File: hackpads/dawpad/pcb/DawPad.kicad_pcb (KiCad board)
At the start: 2 copper layers, 98.5 x 81.5 mm, 32 parts, among them SW1 SW_Push, SW10 SW_Push, SW11 SW_Push, SW12 SW_Push, SW13 RotaryEncoder_Switch_MP, SW14 RotaryEncoder_Switch_MP, SW15 RotaryEncoder_Switch_MP, SW16 RotaryEncoder_Switch_MP, SW2 SW_Push, SW3 SW_Push, SW4 SW_Push, SW5 SW_Push, SW6 SW_Push, SW7 SW_Push, SW8 SW_Push, SW9 SW_Push, U1 XIAO-RP2040-DIP, U2 MCP23017_SO

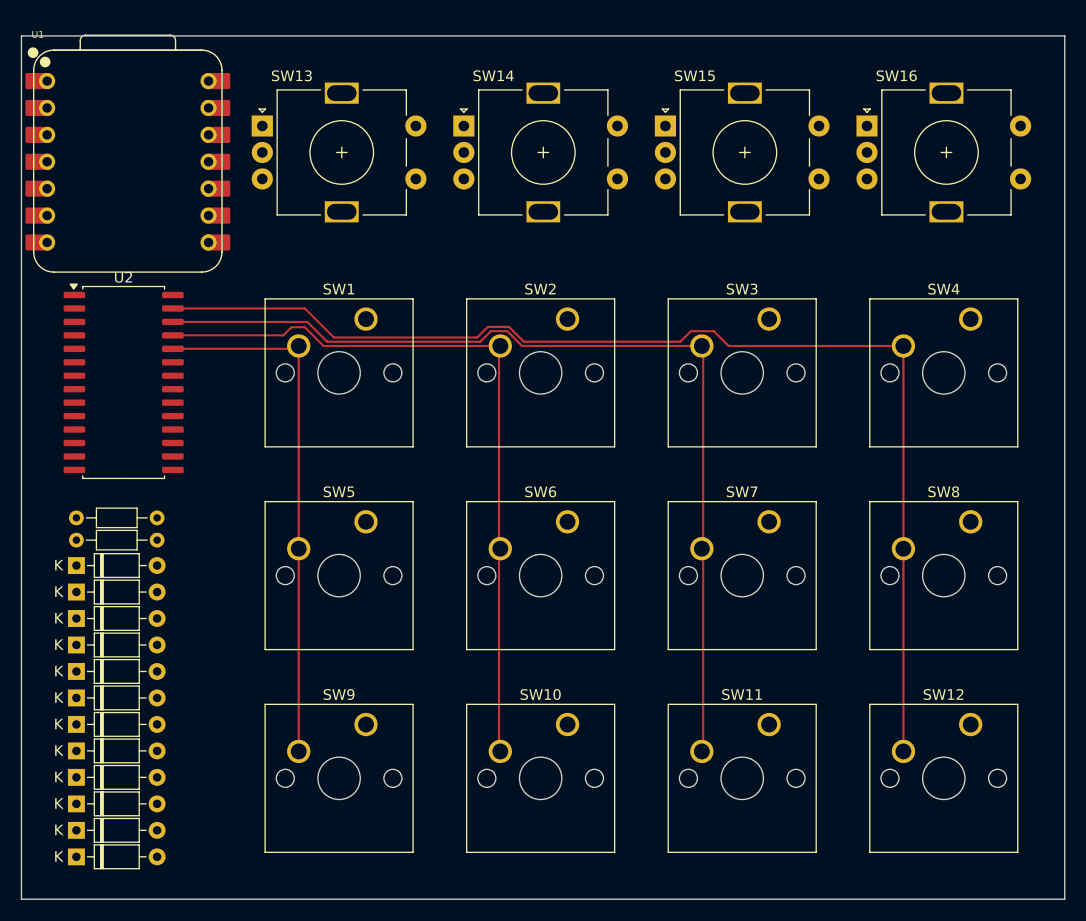
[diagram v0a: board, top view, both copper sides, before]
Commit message: Add LEDs to and finish PCB for DawPad
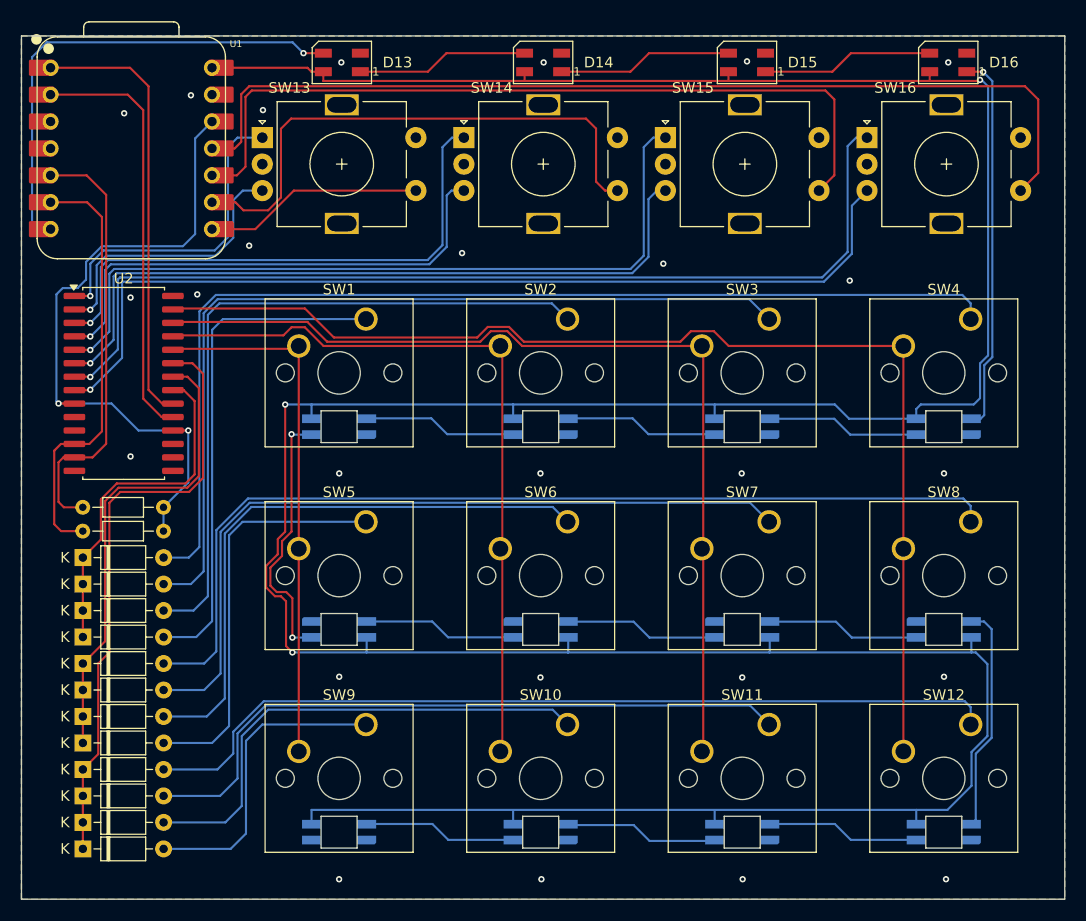
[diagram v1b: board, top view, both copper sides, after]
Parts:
- added D13: SK6812MINI, LED_SMD:LED_SK6812MINI_PLCC4_3.5x3.5mm_P1.75mm, F.Cu at (45.2, 17.5)
- added D14: SK6812MINI, LED_SMD:LED_SK6812MINI_PLCC4_3.5x3.5mm_P1.75mm, F.Cu at (64.2, 17.5)
- added D15: SK6812MINI, LED_SMD:LED_SK6812MINI_PLCC4_3.5x3.5mm_P1.75mm, F.Cu at (83.5, 17.5)
- added D16: SK6812MINI, LED_SMD:LED_SK6812MINI_PLCC4_3.5x3.5mm_P1.75mm, F.Cu at (102.5, 17.5)
- added D17: SK6812MINI, SK6812MINI-E:SK6812MINI-E, B.Cu at (102.1, 51.9)
- added D18: SK6812MINI, SK6812MINI-E:SK6812MINI-E, B.Cu at (83.0, 51.9)
- added D19: SK6812MINI, SK6812MINI-E:SK6812MINI-E, B.Cu at (64.0, 51.9)
- added D20: SK6812MINI, SK6812MINI-E:SK6812MINI-E, B.Cu at (45.0, 51.9)
- added D21: SK6812MINI, SK6812MINI-E:SK6812MINI-E, B.Cu at (45.0, 71.0)
- added D22: SK6812MINI, SK6812MINI-E:SK6812MINI-E, B.Cu at (64.0, 71.0)
- added D23: SK6812MINI, SK6812MINI-E:SK6812MINI-E, B.Cu at (83.0, 71.0)
- added D24: SK6812MINI, SK6812MINI-E:SK6812MINI-E, B.Cu at (102.1, 71.0)
- added D25: SK6812MINI, SK6812MINI-E:SK6812MINI-E, B.Cu at (102.1, 90.2)
- added D26: SK6812MINI, SK6812MINI-E:SK6812MINI-E, B.Cu at (83.0, 90.2)
- added D27: SK6812MINI, SK6812MINI-E:SK6812MINI-E, B.Cu at (64.0, 90.2)
- added D28: SK6812MINI, SK6812MINI-E:SK6812MINI-E, B.Cu at (45.0, 90.2)
- moved D4 18.3 mm to (20.8, 64.2)
- moved D8 13.3 mm to (20.8, 74.2)
- moved D9 11.8 mm to (20.8, 91.8)
- moved D5 9.27 mm to (20.8, 81.8)
- moved R1 8.28 mm to (28.4, 59.5), turned to 180 degrees
- moved D12 8.27 mm to (20.8, 84.2)
- moved R2 8.26 mm to (28.4, 61.8), turned to 180 degrees
- moved D1 6.78 mm to (20.8, 71.8)
- moved D10 4.29 mm to (20.8, 89.2)
- moved D6 4.29 mm to (20.8, 79.2)
- moved D11 3.31 mm to (20.8, 86.8)
- moved D3 3.31 mm to (20.8, 66.8)
- moved D2 1.85 mm to (20.8, 69.2)
- moved U1 1.30 mm to (25.4, 25.6)
- moved SW13 1.10 mm to (37.7, 24.6)
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- renumbered D9 to D10, D8 to D4, D4 to D5, D5 to D6, D6 to D7, D10 to D8, D7 to D9
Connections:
- SW13 pad A: /ENC1_A -> /ENC0_A
- SW13 pad B: /ENC1_B -> /ENC0_B
- SW13 pad S1: /ENC1_SW -> /ENC0_SW
- SW14 pad A: /ENC2_A -> /ENC1_A
- SW14 pad B: /ENC2_B -> /ENC1_B
- SW14 pad S1: /ENC2_SW -> /ENC1_SW
- SW15 pad A: /ENC3_A -> /ENC2_A
- SW15 pad B: /ENC3_B -> /ENC2_B
- SW15 pad S1: /ENC3_SW -> /ENC2_SW
- SW16 pad A: /ENC4_A -> /ENC3_A
- SW16 pad B: /ENC4_B -> /ENC3_B
- SW16 pad S1: /ENC4_SW -> /ENC3_SW
- U1 pad 11: /ENC1_SW -> /ENC3_SW
- U1 pad 7: unconnected-(U1-GPIO0/TX-Pad7) -> /LED_DIN
- U1 pad 8: /ENC4_SW -> /ENC0_SW
- U1 pad 9: /ENC3_SW -> /ENC1_SW
- U2 pad 1: /ENC1_A -> /ENC0_A
- U2 pad 2: /ENC1_B -> /ENC0_B
- U2 pad 3: /ENC2_A -> /ENC1_A
- U2 pad 4: /ENC2_B -> /ENC1_B
- U2 pad 5: /ENC3_A -> /ENC2_A
- U2 pad 6: /ENC3_B -> /ENC2_B
- U2 pad 7: /ENC4_A -> /ENC3_A
- U2 pad 8: /ENC4_B -> /ENC3_B
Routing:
- net +5V: track 0.00 -> 356.6 mm, vias 0 -> 3
- net Net-(D4-A): track 0.00 -> 101.3 mm
- net /ENC3_A: track 0.00 -> 94.0 mm, vias 0 -> 1
- net /ENC3_SW: track 0.00 -> 92.9 mm
- net Net-(D8-A): track 0.00 -> 91.1 mm
- net /ENC3_B: track 0.00 -> 89.5 mm, vias 0 -> 1
- net Net-(D3-A): track 0.00 -> 83.4 mm
- net Net-(D12-A): track 0.00 -> 81.9 mm
- net /ENC2_SW: track 0.00 -> 74.7 mm
- net /ENC2_A: track 0.00 -> 73.3 mm, vias 0 -> 1
- net Net-(D7-A): track 0.00 -> 73.1 mm
- net /ENC2_B: track 0.00 -> 69.4 mm, vias 0 -> 1
- net Net-(D2-A): track 0.00 -> 66.3 mm
- net +3V3: track 0.00 -> 64.8 mm, vias 0 -> 2
- net Net-(D11-A): track 0.00 -> 63.9 mm
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- added copper zone on B.Cu, net GND
- added copper zone on F.Cu, net GND
